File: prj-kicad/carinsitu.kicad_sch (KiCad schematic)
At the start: 78 parts, among them P1 BAT, P2 MOT, P3 CONN_3, P4 CONN_4, Q1 TJ15P04M3, SW1 SWITCH_SLIDE, SW2 Reset, U1 LoLin_D1_mini_pro, U2 MIC2860, U3 MAX17044G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

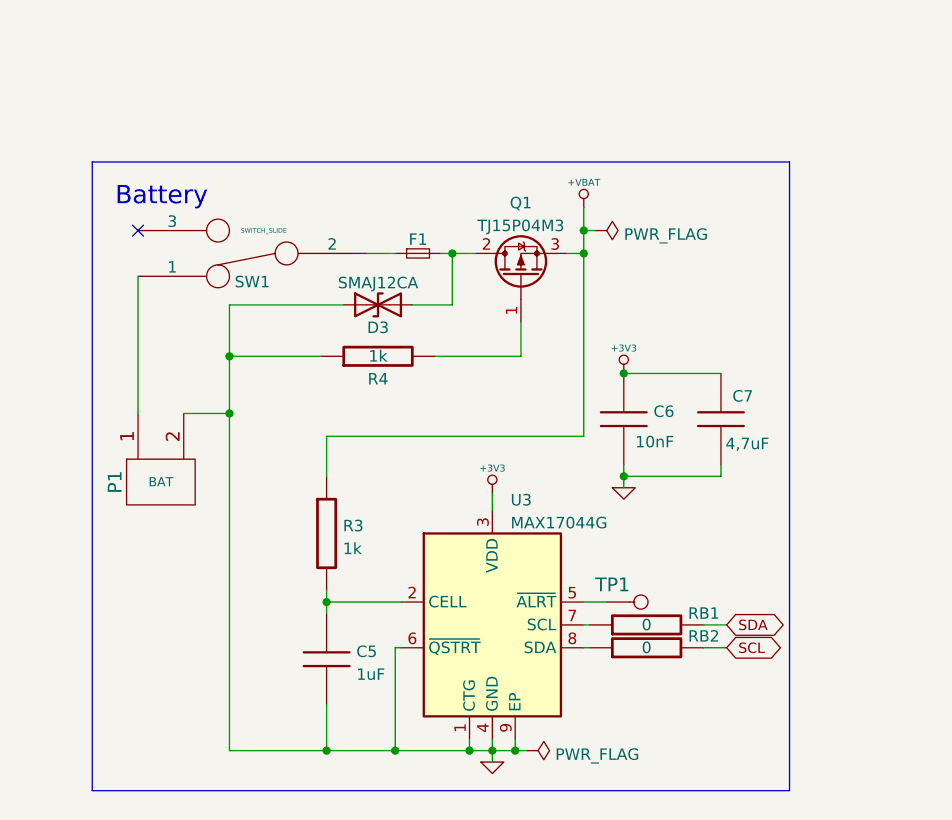
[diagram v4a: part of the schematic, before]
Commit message: use max17261 as battry gauge
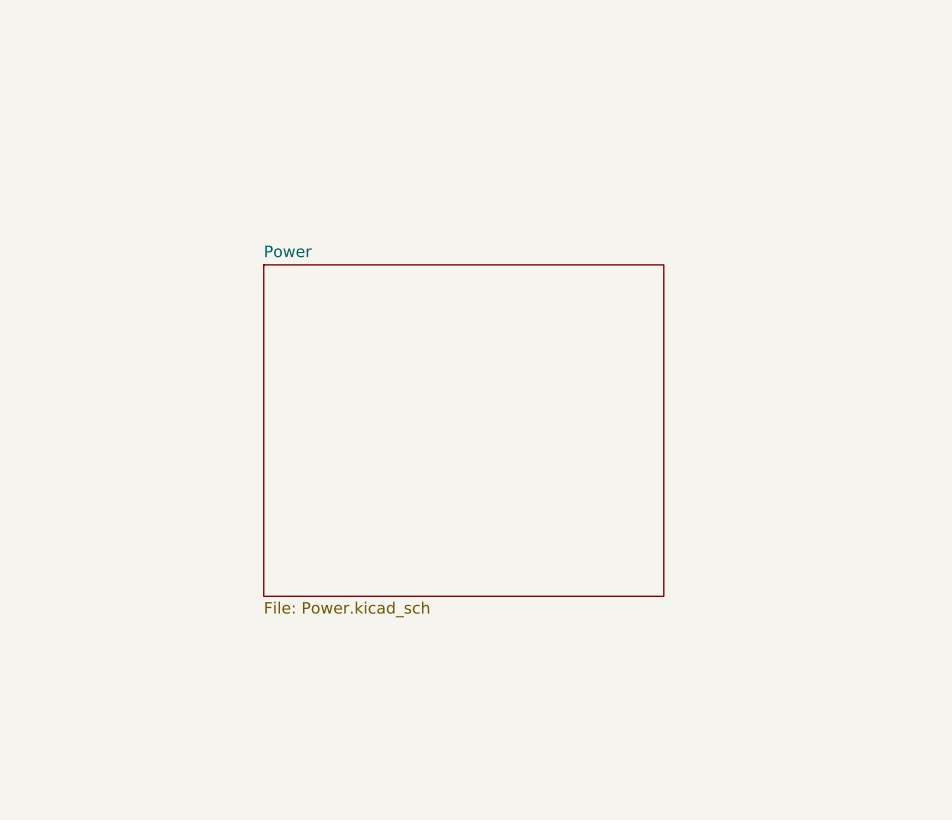
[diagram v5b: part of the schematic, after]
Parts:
- removed C5: 1uF, Capacitor_SMD:C_0805_2012Metric, symbol carinsitu:C
- removed C6: 10nF, Capacitor_SMD:C_0603_1608Metric, symbol carinsitu:C
- removed C7: 4,7uF, Capacitor_SMD:C_0805_2012Metric, symbol carinsitu:C
- removed D3: SMAJ12CA, Diode_SMD:D_SMA, symbol Device:D_TVS
- removed F1: Fuse_Small, Fuse:Fuse_Littelfuse-LVR100, symbol Device:Fuse_Small
- removed P1: BAT, carinsitu:CONN_61300211021, symbol carinsitu:CONN_2
- removed Q1: TJ15P04M3, Package_TO_SOT_SMD:TO-252-2, symbol Device:Q_PMOS_GDS
- removed R3, R4: 1k, Resistor_SMD:R_0805_2012Metric, symbol carinsitu:R
- removed RB1, RB2: 0, Resistor_SMD:R_0603_1608Metric, symbol carinsitu:R
- removed SW1: SWITCH_SLIDE, carinsitu:SW_L102xxxML, symbol carinsitu:SWITCH_SLIDE
- removed TP1: CONN_1, carinsitu:TP, symbol carinsitu:CONN_1
- removed U3: MAX17044G, Package_DFN_QFN:TDFN-8-1EP_3x2mm_P0.5mm_EP1.80x1.65mm, symbol carinsitu:MAX17044G
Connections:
- no-connect marks 4 -> 3
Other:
- added sheet Power (Power.kicad_sch)
- note removed: "Battery"

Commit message: Change schematic to have everything on one page
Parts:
- added C5: 100nF, Capacitor_SMD:C_0603_1608Metric, symbol carinsitu:C
- added C6: 0.47µF, Capacitor_SMD:C_0805_2012Metric, symbol carinsitu:C
- added D3: SMAJ12CA, Diode_SMD:D_SMA, symbol Device:D_TVS
- added F1: Fuse_Small, Fuse:Fuse_Littelfuse-LVR100, symbol Device:Fuse_Small
- added P1: BAT, carinsitu:CONN_61300211021, symbol carinsitu:CONN_2
- added Q1: TJ15P04M3, Package_TO_SOT_SMD:TO-252-2, symbol Device:Q_PMOS_GDS
- added R4: 1k, Resistor_SMD:R_0805_2012Metric, symbol carinsitu:R
- added RB1, RB2: 0, Resistor_SMD:R_0603_1608Metric, symbol carinsitu:R
- added RD1: 800k, Resistor_SMD:R_0603_1608Metric, symbol carinsitu:R
- added RD2: 200k, Resistor_SMD:R_0603_1608Metric, symbol carinsitu:R
- added RSense1: 0.01, Resistor_SMD:R_1210_3225Metric, symbol carinsitu:R
- added SW1: SWITCH_SLIDE, carinsitu:SW_L102xxxML, symbol carinsitu:SWITCH_SLIDE
- added U3: MAX17261xxTD, Package_DFN_QFN:TDFN-14-1EP_3x3mm_P0.4mm_EP1.78x2.35mm, symbol Battery_Management:MAX17261xxTD
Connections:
- net +3V3: now also C5.2, U3.1 (TH), U3.6 (BATT)
- net +VBAT: now also Q1.3 (S), RD1.1
- net GND: now also RSense1.1, U3.7 (CSN)
- net SCL: now also RB1.2
- net SDA: now also RB2.2
- new net: Q1.1 (G), R4.2
- new net: D3.2 (A2), F1.2, Q1.2 (D)
- new net: RB2.1, U3.13 (SDA)
- new net: RD1.2, RD2.2, U3.10 (CELLX)
- new net: P1.1 (P1), SW1.1
- new net: C6.1, U3.11 (REG)
- new net: RB1.1, U3.14 (SCL)
- new net: F1.1, SW1.2
- new net GNDD: C5.1, C6.2, D3.1 (A1), P1.2 (PM), R4.1, RD2.1, RSense1.2, U3.12 (ALRT), U3.15 (GND), U3.8 (GND), U3.9 (CSPL)
- no-connect marks 3 -> 5
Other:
- removed sheet Power
- note added: "+"
- note added: "-"
- note added: "- Battery is 2S Lipo (7.4V nominal, 6.8 to 8.4V) - 5V is generated by ESC module (from battery) - 3V3 is generated by LoLin module (from 5V) - VTX is powered from battery directly"
- note added: "Battery"
- note added: "MCU"
- note added: "Power"
- note added: "Test points and fixations"
- note removed: "Power: - Battery is 2S Lipo (7.4V nominal, 6.8 to 8.4V) - 5V is generated by ESC module (from battery) - 3V3 is generated by LoLin module (from 5V) - VTX is powered from battery directly"
- moved on the sheet: C18, C8, D5, FIX1, FIX2, FIX3, FIX4, FIX5, H1, R1, R10, R6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
